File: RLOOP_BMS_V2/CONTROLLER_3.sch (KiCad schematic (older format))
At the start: 32 parts, among them U1 bq76PL536A_HTQFP

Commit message: More WIP
Added connector for 1-Wire sensors if we want to put some sensors on the
heat-sinks. Just need to double check everything with the 3d-models.
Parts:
- U1: symbol bq76PL536A_HTQFP -> bq76PL536A_HTQFP-RESCUE-rLoop_BMS_v2
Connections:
- wire segments 126 -> 127
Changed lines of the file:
@@
 EESchema Schematic File Version 2
+LIBS:rLoop BMS v2-rescue
 LIBS:power
 LIBS:device
@@
 	6550 3600 6850 3600
 Connection ~ 6850 3600
-Text GLabel 4100 2800 0    60   Input ~ 0
+Text GLabel 3950 2800 0    60   Input ~ 0
 GND_3
 Wire Wire Line
@@
 	4300 2900 4200 2900
 Wire Wire Line
-	4200 2800 4200 3000
+	4200 2700 4200 3000
 Connection ~ 4200 2800
 Wire Wire Line
@@
 	1900 6650 2050 6650
 Wire Wire Line
-	2050 6850 1900 6850
+	1900 6850 2050 6850
 Wire Wire Line
 	5900 4350 5900 5850
@@
 $EndComp
 $Comp
-L bq76PL536A_HTQFP U1
+L bq76PL536A_HTQFP-RESCUE-rLoop_BMS_v2 U1
 U 1 1 592A87C5
 P 5450 2900
+AR Path="/592A87C5" Ref="U1"  Part="1"
+AR Path="/590C6B15/592A87C5" Ref="U1"  Part="1"
 F 0 "U1" H 5450 2900 60  0000 C CNN
 F 1 "bq76PL536A_HTQFP" H 5450 3150 60  0000 C CNN
@@
 	1950 7000 1950 6850
 Connection ~ 1950 6850
+Wire Wire Line
+	4300 2700 4200 2700
 $EndSCHEMATC

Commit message: more WIP
So close. Need to finish arranging the sild screen and make sure diodes
get put on in the correct orientation.
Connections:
- net GND_3: now also U1.THRM
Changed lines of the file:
@@
 	6550 3500 6850 3500
 Wire Wire Line
-	6850 3500 6850 4150
+	6850 3400 6850 4150
 Wire Wire Line
 	6550 3600 6850 3600
@@
 Wire Wire Line
 	4300 2700 4200 2700
+Wire Wire Line
+	6550 3400 6850 3400
+Connection ~ 6850 3500
 $EndSCHEMATC

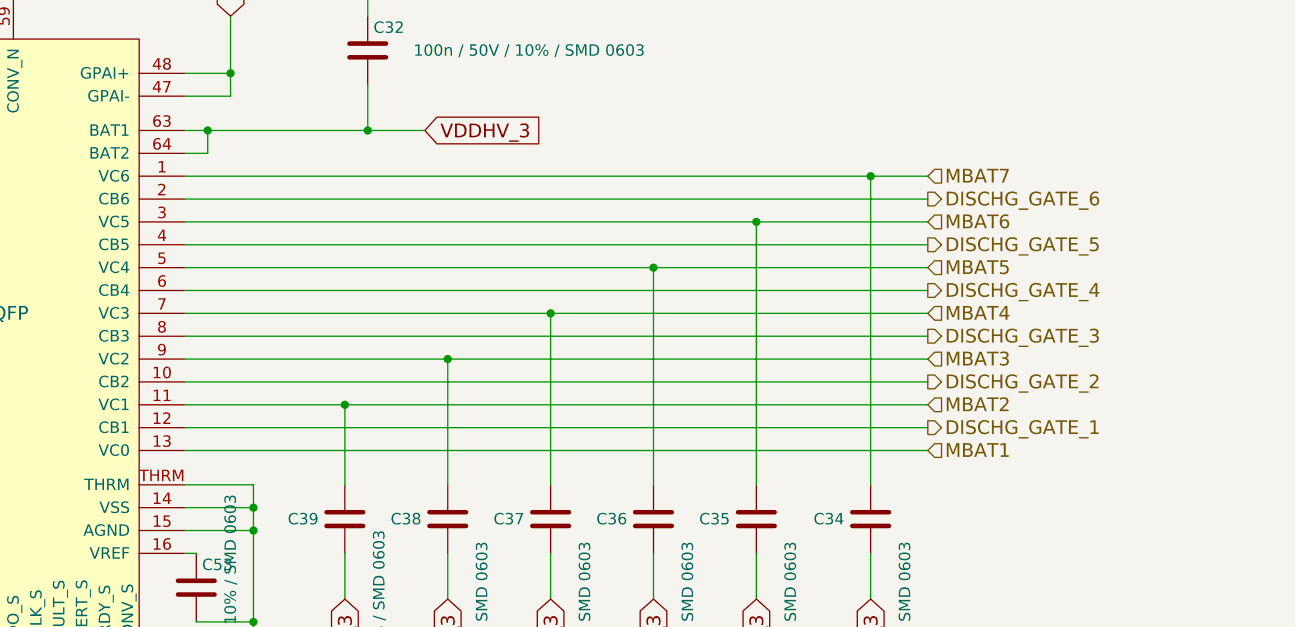
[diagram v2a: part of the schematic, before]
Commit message: Updated page sizes for schematics
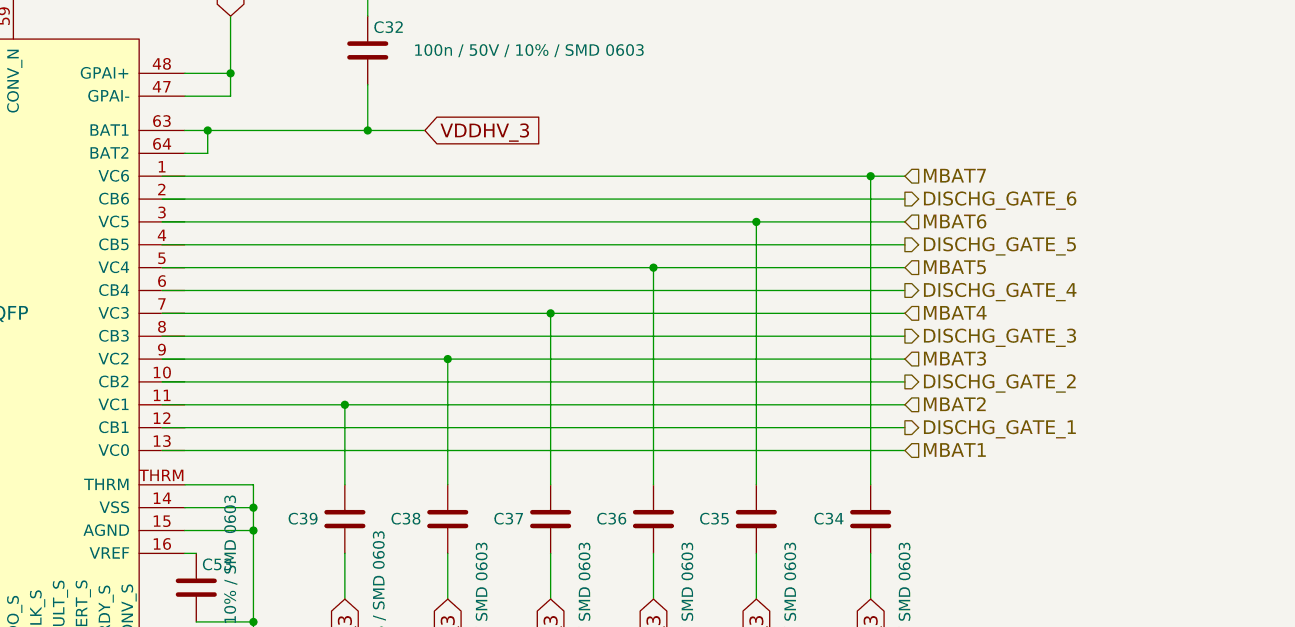
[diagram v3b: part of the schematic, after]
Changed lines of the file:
@@
 EELAYER 25 0
 EELAYER END
-$Descr A4 11693 8268
+$Descr USLetter 11000 8500
 encoding utf-8
 Sheet 4 10
@@
 Comment4 ""
 $EndDescr
-Text HLabel 9800 3250 2    60   Input ~ 0
+Text HLabel 9700 3250 2    60   Input ~ 0
 MBAT1
-Text HLabel 9800 3050 2    60   Input ~ 0
+Text HLabel 9700 3050 2    60   Input ~ 0
 MBAT2
-Text HLabel 9800 2850 2    60   Input ~ 0
+Text HLabel 9700 2850 2    60   Input ~ 0
 MBAT3
-Text HLabel 9800 2650 2    60   Input ~ 0
+Text HLabel 9700 2650 2    60   Input ~ 0
 MBAT4
-Text HLabel 9800 2450 2    60   Input ~ 0
+Text HLabel 9700 2450 2    60   Input ~ 0
 MBAT5
-Text HLabel 9800 2250 2    60   Input ~ 0
+Text HLabel 9700 2250 2    60   Input ~ 0
 MBAT6
-Text HLabel 9800 2050 2    60   Input ~ 0
+Text HLabel 9700 2050 2    60   Input ~ 0
 MBAT7
-Text HLabel 9800 3150 2    60   Output ~ 0
+Text HLabel 9700 3150 2    60   Output ~ 0
 DISCHG_GATE_1
-Text HLabel 9800 2950 2    60   Output ~ 0
+Text HLabel 9700 2950 2    60   Output ~ 0
 DISCHG_GATE_2
-Text HLabel 9800 2750 2    60   Output ~ 0
+Text HLabel 9700 2750 2    60   Output ~ 0
 DISCHG_GATE_3
-Text HLabel 9800 2550 2    60   Output ~ 0
+Text HLabel 9700 2550 2    60   Output ~ 0
 DISCHG_GATE_4
-Text HLabel 9800 2350 2    60   Output ~ 0
+Text HLabel 9700 2350 2    60   Output ~ 0
 DISCHG_GATE_5
-Text HLabel 9800 2150 2    60   Output ~ 0
+Text HLabel 9700 2150 2    60   Output ~ 0
 DISCHG_GATE_6
 Text HLabel 5700 5850 3    60   Input ~ 0
@@
 	9550 3700 9550 3900
 Wire Wire Line
-	6550 2050 9800 2050
-Wire Wire Line
-	9800 2150 6550 2150
-Wire Wire Line
-	6550 2250 9800 2250
-Wire Wire Line
-	9800 2350 6550 2350
-Wire Wire Line
-	6550 2450 9800 2450
-Wire Wire Line
-	6550 2550 9800 2550
-Wire Wire Line
-	6550 2650 9800 2650
-Wire Wire Line
-	6550 2750 9800 2750
-Wire Wire Line
-	6550 2850 9800 2850
-Wire Wire Line
-	6550 2950 9800 2950
-Wire Wire Line
-	6550 3050 9800 3050
-Wire Wire Line
-	6550 3150 9800 3150
-Wire Wire Line
-	9800 3250 6550 3250
+	6450 2050 9700 2050
+Wire Wire Line
+	9700 2150 6450 2150
+Wire Wire Line
+	6450 2250 9700 2250
+Wire Wire Line
+	9700 2350 6450 2350
+Wire Wire Line
+	6450 2450 9700 2450
+Wire Wire Line
+	6450 2550 9700 2550
+Wire Wire Line
+	6450 2650 9700 2650
+Wire Wire Line
+	6450 2750 9700 2750
+Wire Wire Line
+	6450 2850 9700 2850
+Wire Wire Line
+	6450 2950 9700 2950
+Wire Wire Line
+	6450 3050 9700 3050
+Wire Wire Line
+	6450 3150 9700 3150
+Wire Wire Line
+	9700 3250 6450 3250
 Wire Wire Line
 	9550 3400 9550 2050

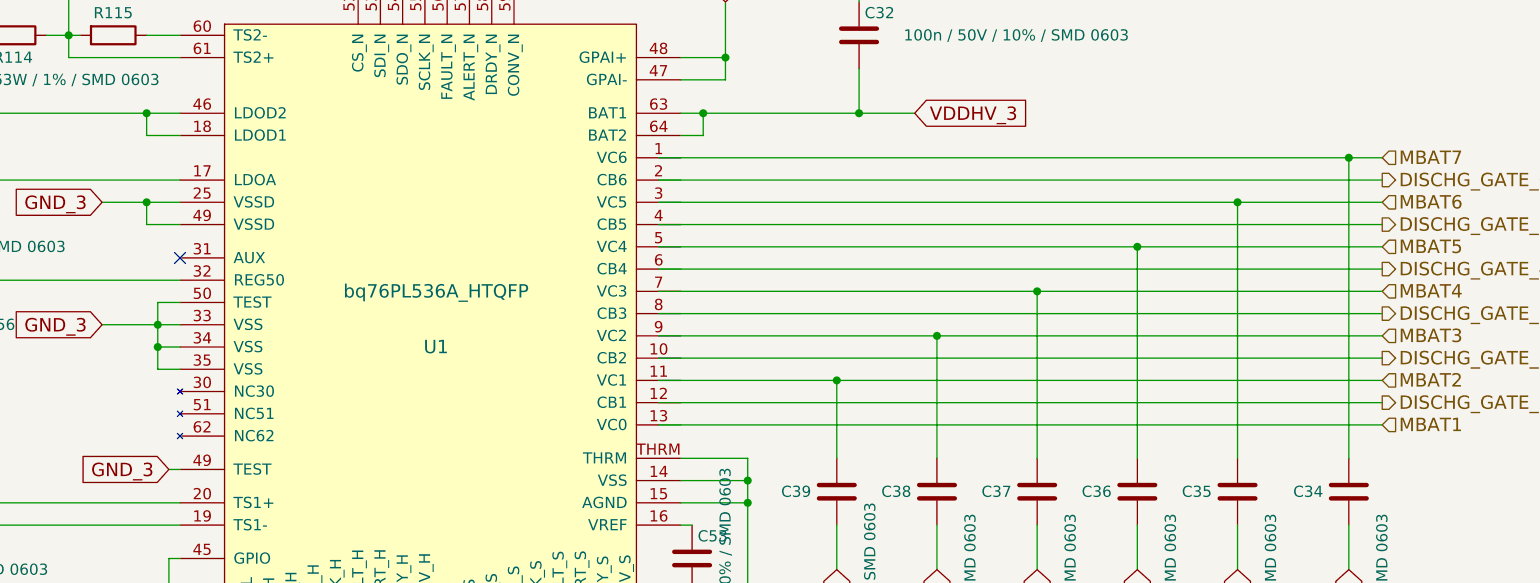
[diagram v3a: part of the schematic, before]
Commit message: swapped a few connectors to standardize with the power node and what's readily available
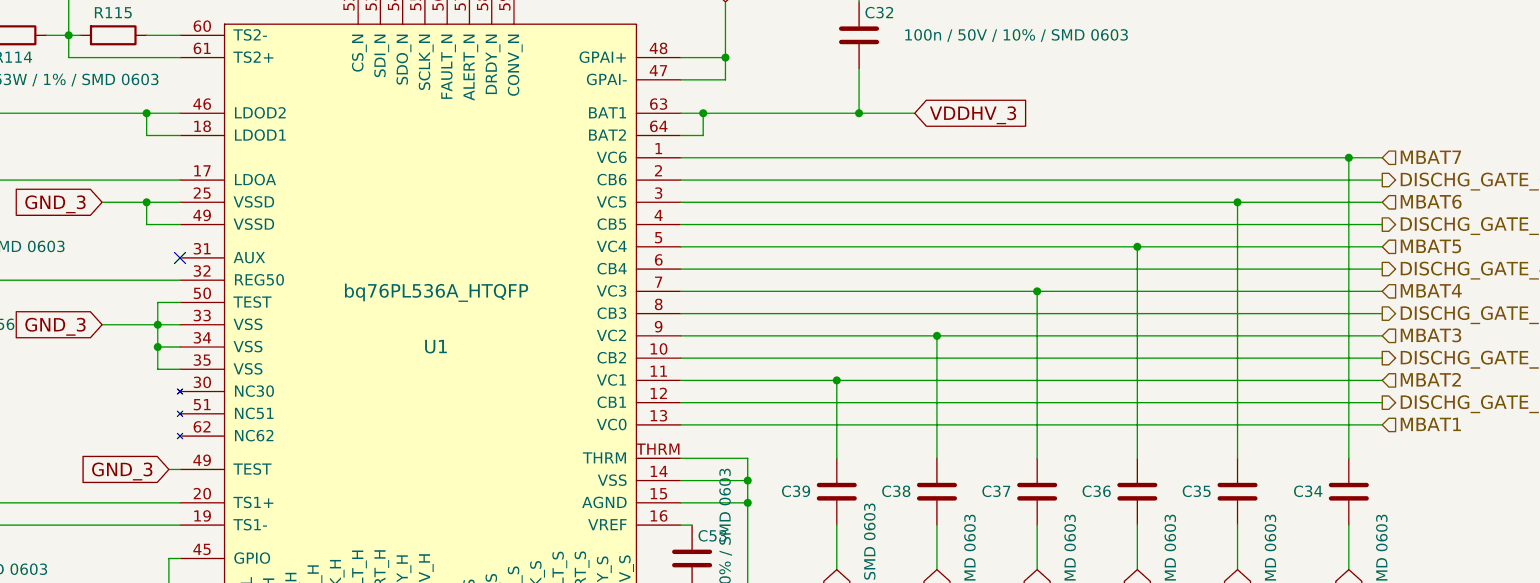
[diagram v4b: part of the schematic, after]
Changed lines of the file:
@@
 	9550 3700 9550 3900
 Wire Wire Line
-	6450 2050 9700 2050
-Wire Wire Line
-	9700 2150 6450 2150
-Wire Wire Line
-	6450 2250 9700 2250
-Wire Wire Line
-	9700 2350 6450 2350
-Wire Wire Line
-	6450 2450 9700 2450
-Wire Wire Line
-	6450 2550 9700 2550
-Wire Wire Line
-	6450 2650 9700 2650
-Wire Wire Line
-	6450 2750 9700 2750
-Wire Wire Line
-	6450 2850 9700 2850
-Wire Wire Line
-	6450 2950 9700 2950
-Wire Wire Line
-	6450 3050 9700 3050
-Wire Wire Line
-	6450 3150 9700 3150
-Wire Wire Line
-	9700 3250 6450 3250
+	6550 2050 9700 2050
+Wire Wire Line
+	6550 2250 9700 2250
+Wire Wire Line
+	6550 2450 9700 2450
+Wire Wire Line
+	6550 2650 9700 2650
 Wire Wire Line
 	9550 3400 9550 2050
@@
 	3950 2800 4300 2800
 Wire Wire Line
-	4300 2900 4200 2900
+	4200 2900 4300 2900
 Wire Wire Line
 	4200 2700 4200 3000
@@
 	6550 3400 6850 3400
 Connection ~ 6850 3500
+Wire Wire Line
+	6550 2150 9700 2150
+Wire Wire Line
+	6550 2350 9700 2350
+Wire Wire Line
+	6550 2550 9700 2550
+Wire Wire Line
+	6550 2750 9700 2750
+Wire Wire Line
+	9700 2850 6550 2850
+Wire Wire Line
+	6550 2950 9700 2950
+Wire Wire Line
+	9700 3050 6550 3050
+Wire Wire Line
+	6550 3150 9700 3150
+Wire Wire Line
+	9700 3250 6550 3250
 $EndSCHEMATC
